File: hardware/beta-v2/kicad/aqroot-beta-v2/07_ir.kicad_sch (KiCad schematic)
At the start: 9 parts, among them Q1 AO3400A, U6 TSOP38238

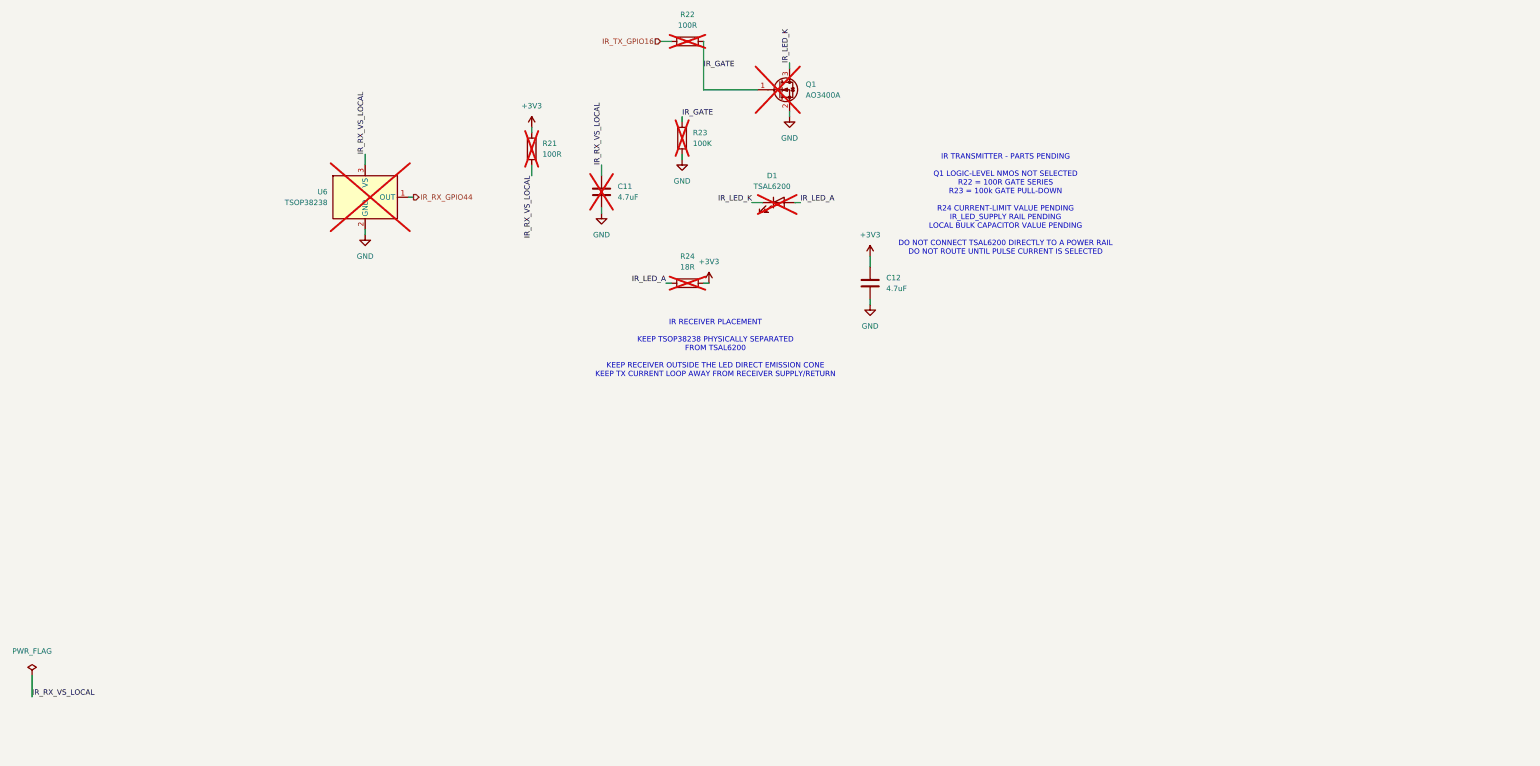
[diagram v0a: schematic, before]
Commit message: hardware: migrate Full Beta v2 infrared (FBV2-S1-007)
Sheet 07. Task gate FBV2-S1-IR = PASS.
ERC 45 -> 45: zero added, zero removed. Errors remain 2, both inherited.

THE WHOLE IR SUBSYSTEM ARRIVED DNP - FOR THE FOURTH SHEET RUNNING.

U6, D1, Q1, R21, R22, R23, R24 and C11 all came from Beta-DM marked DNP. Only
C12 was fitted - decoupling for a transmitter that was not there, exactly the
pattern found on sheet 06 with C9/C10 and the MAX98357A. The brief opens with
"Full Beta v2 IR is a mandatory internal feature", so all eight are now fitted.

Sheet 09's U16/R49/R50/U15/D2/D3, sheet 06's U5/J6, now all of sheet 07. This is
no longer a coincidence: a DNP on a Beta-DM sheet describes what was populated on
that reduced build, not what the architecture requires. Sheets 08 and 09 must be
assumed to carry the same trap.

THE RATING THAT BINDS IS NOT THE ONE THAT LOOKS BIGGEST.

IFSM = 1.5 A is a SINGLE-PULSE surge for t <= 5 us. It is not a remote-control
rating and cannot justify carrier current. The figure that governs a 38 kHz burst
train is IFM = 200 mA, specified at tp/T = 0.5 with tp = 100 us - a LONGER pulse
at the same duty than a 38 kHz carrier produces, so the carrier is less stressful
than the specified condition, not more.

Duty model, standard NEC frame ~67.5 ms with the carrier active ~22 ms at one
third duty, so the LED is on ~11 % of a frame:

  100 mA   50 % of IFM   15 mW avg   dTj 3.4 K   safe, leaves range on the table
  150 mA   75 % of IFM   25 mW avg   dTj 5.7 K   SELECTED
  200 mA  100 % of IFM   35 mW avg   dTj 8.1 K   no tolerance margin left
  300 mA  150 % of IFM        -           -      REJECTED, out of spec

Thermally none of these is difficult - 25 mW against a 160 mW PV limit on a
230 K/W part. The constraint is the repetitive rating and it is hard. Range is
not the constraint either: the TSOP384xx datasheet quotes 45 m transmission
distance using a TSAL6200 at only IF = 50 mA, and the TSAL6100 at 150 mA is
roughly 20x that intensity. Curr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
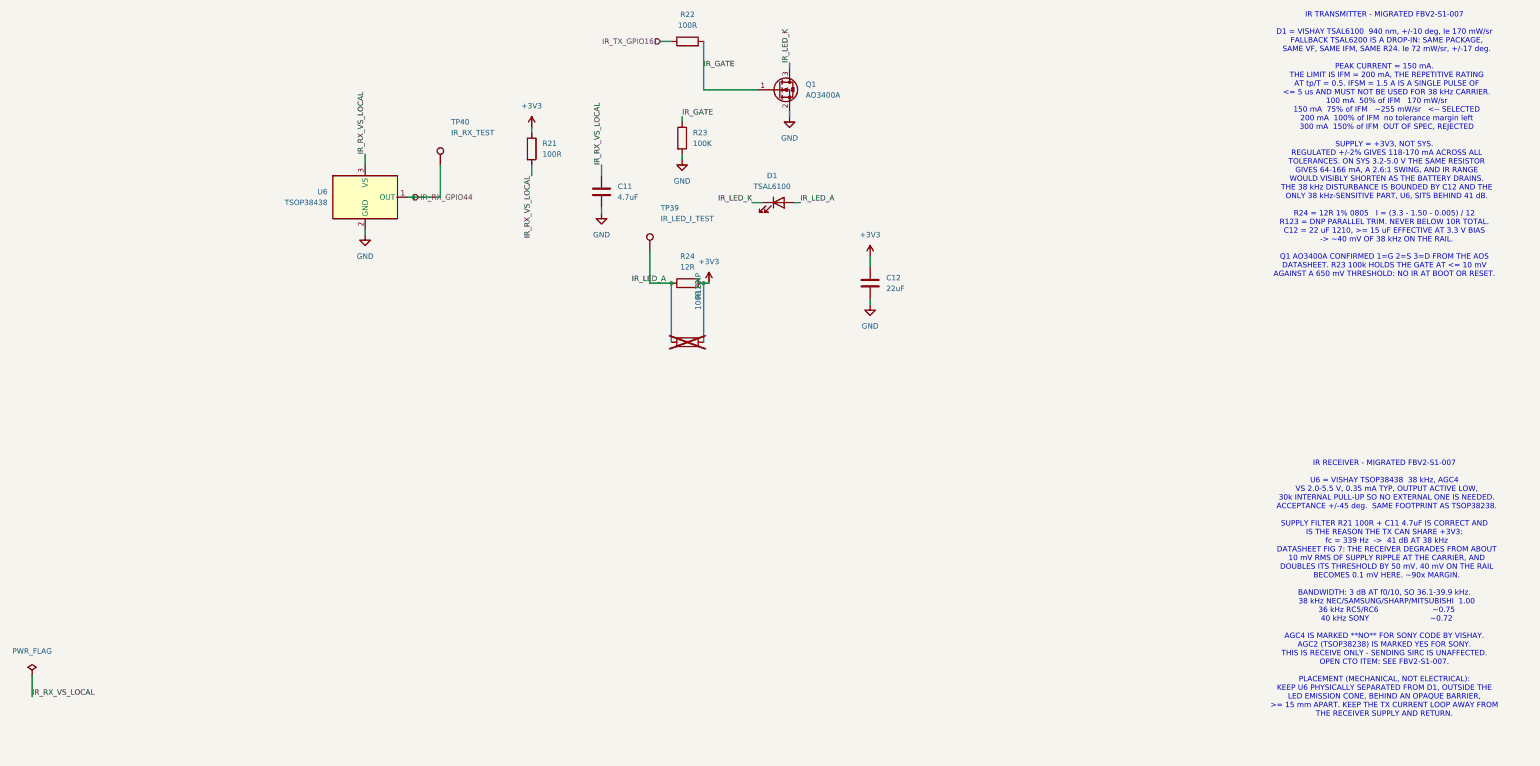
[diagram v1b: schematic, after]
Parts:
- added R123: 100R DNP, Resistor_SMD:R_0805_2012Metric, symbol Device:R
- added TP39: IR_LED_I_TEST, TestPoint:TestPoint_Pad_D1.0mm, symbol Connector:TestPoint
- added TP40: IR_RX_TEST, TestPoint:TestPoint_Pad_D1.0mm, symbol Connector:TestPoint
- C11: Note (none) -> IR RECEIVER SUPPLY FILTER, shunt element. RETAINED at 4.7 u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; now fitted
- C12: value 4.7uF -> 22uF; footprint Capacitor_SMD:C_0805_2012Metric -> Capacitor_SMD:C_1210_3225Metric; Note Local IR pulse reservoir on the +3V3 IR LED branch; supplie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 -> LOCAL IR RESERVOIR, re-derived in FBV2-S1-007. 4.7 uF -> 22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; Package 0805 (2012 metric) -> 1210 (3225 metric); Voltage 10V -> 16V
- D1: value TSAL6200 -> TSAL6100; MPN (none) -> TSAL6100; Manufacturer (none) -> Vishay; Note (none) -> IR EMITTER LOCKED TSAL6100 in FBV2-S1-007, replacing the in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; Package (none) -> T-1 3/4 leaded, 5 mm diameter, 2.54 mm lead pitch; now fitted
- Q1: Note IR LED low-side driver. Symbol Transistor_FET:Q_NMOS_GSD ma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 -> IR LED low-side driver, RETAINED after audit in FBV2-S1-007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; Package SOT-23-3 - LOCKED. Footprint BLOCKED: needs the official AO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 -> SOT-23-3, pin 1 = G, 2 = S, 3 = D (confirmed from the AOS d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; now fitted
- R21: Note (none) -> IR RECEIVER SUPPLY FILTER, series element. RETAINED at 100 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; now fitted
- R22: Note (none) -> IR gate series resistor. RETAINED at 100 R. It damps the ga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; now fitted
- R23: Note (none) -> IR gate pull-down. RETAINED at 100 k. This is the safe-OFF 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; now fitted
- R24: value 18R -> 12R; Note IR LED current limit on the +3V3 IR branch. Rail 3.3 V, TSA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 -> IR LED CURRENT LIMIT, re-derived in FBV2-S1-007 for a 150 m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; now fitted
- U6: value TSOP38238 -> TSOP38438; symbol AQROOT_Beta:TSOP38238 -> AQROOT_Beta:TSOP38438; MPN TSOP38238 -> TSOP38438; Note (none) -> RECEIVER MPN CHANGED TSOP38238 -> TSOP38438 in FBV2-S1-007 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; Package (none) -> Minicast leaded, 5.0 W x 6.95 H x 4.8 D mm, 1 = OUT, 2 = GN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; now fitted
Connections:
- net +3V3: now also R123.2
- net IR_LED_A: now also R123.1, TP39.1
- net IR_RX_GPIO44: now also TP40.1
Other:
- note added: "IR RECEIVER - MIGRATED FBV2-S1-007 U6 = VISHAY TSOP38438 38 kHz, AGC4 VS 2.0-5.5 V, 0.35 mA TYP, OUTPUT ACTIVE LOW, 30k INTERNAL PULL-UP SO NO EXTERNAL ONE IS NEEDED. ACCEPTANCE +/-45 deg. SAME FOOTPRINT AS TSOP38238. SUPPLY FILTER R21 100R + C11 4.7uF IS CORRECT AND IS THE REASON THE TX CAN SHARE +3V3: fc = 339 Hz -> 41 dB AT 38 kHz DATASHEET FIG 7: THE RECEIVER DEGRADES FROM ABOUT 10 mV RMS OF 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"
- note added: "IR TRANSMITTER - MIGRATED FBV2-S1-007 D1 = VISHAY TSAL6100 940 nm, +/-10 deg, Ie 170 mW/sr FALLBACK TSAL6200 IS A DROP-IN: SAME PACKAGE, SAME VF, SAME IFM, SAME R24. Ie 72 mW/sr, +/-17 deg. PEAK CURRENT = 150 mA. THE LIMIT IS IFM = 200 mA, THE REPETITIVE RATING AT tp/T = 0.5. IFSM = 1.5 A IS A SINGLE PULSE OF <= 5 us AND MUST NOT BE USED FOR 38 kHz CARRIER. 100 mA 50% of IFM 170 mW/sr 150 mA 75% 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"
- note removed: "IR RECEIVER PLACEMENT KEEP TSOP38238 PHYSICALLY SEPARATED FROM TSAL6200 KEEP RECEIVER OUTSIDE THE LED DIRECT EMISSION CONE KEEP TX CURRENT LOOP AWAY FROM RECEIVER SUPPLY/RETURN"
- note removed: "IR TRANSMITTER - PARTS PENDING Q1 LOGIC-LEVEL NMOS NOT SELECTED R22 = 100R GATE SERIES R23 = 100k GATE PULL-DOWN R24 CURRENT-LIMIT VALUE PENDING IR_LED_SUPPLY RAIL PENDING LOCAL BULK CAPACITOR VALUE PENDING DO NOT CONNECT TSAL6200 DIRECTLY TO A POWER RAIL DO NOT ROUTE UNTIL PULSE CURRENT IS SELECTED"

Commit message: hardware: migrate Full Beta v2 buttons expanders and RGB status
Sheet 08 migrated (FBV2-S1-008), resumed after a session-limit interruption.
All prior work was uncommitted working-tree change; it was inspected, kept and
finished rather than restarted.

Both expanders are NXP PCAL9535APW,118, verified against PCAL9535A Rev. 2
(23-Jan-2015) and NOT treated as a behavioural drop-in: it powers up with every
interrupt masked, the opposite of the TCA9535. U2 = 0x20, U3 = 0x21 preserved.

The two-expander allocation genuinely fails: 35 committed signals against 32
pins, with zero free native GPIO (so the WS2812 escape is impossible),
RESERVED_SPARE mandated by D-094 and ten XGPIO locked by D-082. Closed by U23,
a third PCAL9535APW,118 at 0x22 carrying only the front RGB and the reserved
spare - no new MPN, no new footprint, no new driver, no new rail, and B-37
retired with 12 spare I/O. Core, community and safety functions are placed
before the RGB by construction.

Landed: BQ25185_STAT1/STAT2 (10k pull-ups), SD_CARD_DETECT_N, TOUCH_INT_N,
SX1262_DIO1 on U2; ACC_3V3_EN, ACC_5V_EN, ACC_DETECT_N, ACC_POWER_FAULT_N on
U3. RESERVED_SPARE created on U23 P03 with R130 and TP41 - it had never existed.

Front RGB: D13 MEIHUA MHPA3528RGBCT (LCSC C409779), common anode, R124 1k /
R125 680R / R126 390R = 1.50 / 1.03 / 1.67 mA, white 4.20 mA. Dark by
construction with no external pull-ups.

IR receiver reverted to TSOP38238 (AGC2), TSOP38438 retained as a documented
drop-in fallback. Closes O-5.

Sheets 01 and 03 touched only to promote six local labels to hierarchical so
the required nets could reach the expanders; no component, value, topology or
DNP state changed.

ERC 42 messages / 1 error / 41 warnings - identical violation set to the
recovered tree and better than the 45/2/43 pre-sheet-08 baseline. Zero new
errors. fork_equivalence.py PASS, netclass_probe.py PASS, PCB still
bit-identical to Beta-DM. Sheet 09 untouched.

Co-Authored-By: Claude Opus 5 <noreply@anthropic.com>
Claud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
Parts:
- U6: value TSOP38438 -> TSOP38238; symbol AQROOT_Beta:TSOP38438 -> AQROOT_Beta:TSOP38238; MPN TSOP38438 -> TSOP38238; Note RECEIVER MPN CHANGED TSOP38238 -> TSOP38438 in FBV2-S1-007 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 -> RECEIVER REVERTED TSOP38438 -> TSOP38238 in FBV2-S1-008 by 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
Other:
- note added: "IR RECEIVER - MIGRATED FBV2-S1-007 RECEIVER CORRECTED FBV2-S1-008 U6 = VISHAY TSOP38238 38 kHz, AGC2 VS 2.0-5.5 V, 0.35 mA TYP, OUTPUT ACTIVE LOW, 30k INTERNAL PULL-UP SO NO EXTERNAL ONE IS NEEDED. ACCEPTANCE +/-45 deg. TSOP38438 (AGC4) IS A DOCUMENTED DROP-IN FALLBACK: SAME MINICAST BODY, SAME 1=OUT/2=GND/3=VS PINNING, SAME FOOTPRINT, SAME ELECTRICAL TABLE. SUPPLY FILTER R21 100R + C11 4.7uF IS 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"
- note removed: "IR RECEIVER - MIGRATED FBV2-S1-007 U6 = VISHAY TSOP38438 38 kHz, AGC4 VS 2.0-5.5 V, 0.35 mA TYP, OUTPUT ACTIVE LOW, 30k INTERNAL PULL-UP SO NO EXTERNAL ONE IS NEEDED. ACCEPTANCE +/-45 deg. SAME FOOTPRINT AS TSOP38238. SUPPLY FILTER R21 100R + C11 4.7uF IS CORRECT AND IS THE REASON THE TX CAN SHARE +3V3: fc = 339 Hz -> 41 dB AT 38 kHz DATASHEET FIG 7: THE RECEIVER DEGRADES FROM ABOUT 10 mV RMS OF 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"
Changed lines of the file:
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@@
 		)
 	)
-	(text "IR RECEIVER - MIGRATED FBV2-S1-007\n\nU6 = VISHAY TSOP38438  38 kHz, AGC4\n  VS 2.0-5.5 V, 0.35 mA TYP, OUTPUT ACTIVE LOW,\n  30k INTERNAL PULL-UP SO NO EXTERNAL ONE IS NEEDED.\n  ACCEPTANCE +/-45 deg.  SAME FOOTPRINT AS TSOP38238.\n\nSUPPLY FILTER R21 100R + C11 4.7uF IS CORRECT AND\nIS THE REASON THE TX CAN SHARE +3V3:\n  fc = 339 Hz  ->  41 dB AT 38 kHz\n  DATASHEET FIG 7: THE RECEIVER DEGRADES FROM ABOUT\n  10 mV RMS OF SUPPLY RIPPLE AT THE CARRIER, AND\n  DOUBLES ITS THRESHOLD BY 50 mV. 40 mV ON THE RAIL\n  BECOMES 0.1 mV HERE. ~90x MARGIN.\n\nBANDWIDTH: 3 dB AT f0/10, SO 36.1-39.9 kHz.\n  38 kHz NEC/SAMSUNG/SHARP/MITSUBISHI  1.00\n  36 kHz RC5/RC6                       ~0.75\n  40 kHz SONY                          ~0.72\n\nAGC4 IS MARKED **NO** FOR SONY CODE BY VISHAY.\nAGC2 (TSOP38238) IS MARKED YES FOR SONY.\nTHIS IS RECEIVE ONLY - SENDING SIRC IS UNAFFECTED.\nOPEN CTO ITEM: SEE FBV2-S1-007.\n\nPLACEMENT (MECHANICAL, NOT ELECTRICAL):\nKEEP U6 PHYSICALLY SEPARATED FROM D1, OUTSIDE THE\nLED EMISSION CONE, BEHIND AN OPAQUE BARRIER,\n>= 15 mm APART. KEEP THE TX CURRENT LOOP AWAY FROM\nTHE RECEIVER SUPPLY AND RETURN."
+	(text "IR RECEIVER - MIGRATED FBV2-S1-007\nRECEIVER CORRECTED FBV2-S1-008\n\nU6 = VISHAY TSOP38238  38 kHz, AGC2\n  VS 2.0-5.5 V, 0.35 mA TYP, OUTPUT ACTIVE LOW,\n  30k INTERNAL PULL-UP SO NO EXTERNAL ONE IS NEEDED.\n  ACCEPTANCE +/-45 deg.\n  TSOP38438 (AGC4) IS A DOCUMENTED DROP-IN FALLBACK:\n  SAME MINICAST BODY, SAME 1=OUT/2=GND/3=VS PINNING,\n  SAME FOOTPRINT, SAME ELECTRICAL TABLE.\n\nSUPPLY FILTER R21 100R + C11 4.7uF IS CORRECT AND\nIS THE REASON THE TX CAN SHARE +3V3:\n  fc = 339 Hz  ->  41 dB AT 38 kHz\n  DATASHEET FIG 7: THE RECEIVER DEGRADES FROM ABOUT\n  10 mV RMS OF SUPPLY RIPPLE AT THE CARRIER, AND\n  DOUBLES ITS THRESHOLD BY 50 mV. 40 mV ON THE RAIL\n  BECOMES 0.1 mV HERE. ~90x MARGIN.\n\nBANDWIDTH: 3 dB AT f0/10, SO 36.1-39.9 kHz.\n  38 kHz NEC/SAMSUNG/SHARP/MITSUBISHI  1.00\n  36 kHz RC5/RC6                       ~0.75\n  40 kHz SONY                          ~0.72\n\nO-5 IS CLOSED. THE CTO RULED FOR AGC2.\nAGC2 IS MARKED YES FOR ALL SIX LISTED PROTOCOLS\nINCLUDING SONY; AGC4 IS MARKED **NO** FOR SONY.\nMECHANISM: AFTER A BURST > 10 CYCLES AGC2 NEEDS A\nGAP > 5x THE BURST AND TAKES 10-70 CYCLES/BURST,\nAGC4 NEEDS > 15x AND TAKES ONLY 10-35. SIRC BREAKS\nTHE AGC4 LIMIT.\nCOST OF THE REVERT: AGC4 FIG 15 HIGH-MODULATION\nFLUORESCENT SUPPRESSION IS LOST. AGC2 HAS FIG 14.\n\nPLACEMENT (MECHANICAL, NOT ELECTRICAL):\nKEEP U6 PHYSICALLY SEPARATED FROM D1, OUTSIDE THE\nLED EMISSION CONE, BEHIND AN OPAQUE BARRIER,\n>= 15 mm APART. KEEP THE TX CURRENT LOOP AWAY FROM\nTHE RECEIVER SUPPLY AND RETURN."
 		(exclude_from_sim no)
 		(at 340 165 0)
@@
 	)
 	(symbol
-		(lib_id "AQROOT_Beta:TSOP38438")
+		(lib_id "AQROOT_Beta:TSOP38238")
 		(at 99.06 72.39 0)
 		(unit 1)
@@
 			)
 		)
-		(property "Value" "TSOP38438"
+		(property "Value" "TSOP38238"
 			(at 90.17 73.6599 0)
 			(show_name no)
@@
 			)
 		)
-		(property "Description" "38 kHz IR remote-control receiver module, AGC4"
+		(property "Description" "38 kHz IR remote-control receiver module, AGC2"
 			(at 99.06 72.39 0)
 			(hide yes)
@@
 			)
 		)
-		(property "MPN" "TSOP38438"
+		(property "MPN" "TSOP38238"
 			(at 99.06 72.39 0)
 			(hide yes)
@@
 			)
 		)
-		(property "Note" "RECEIVER MPN CHANGED TSOP38238 -> TSOP38438 in FBV2-S1-007 per the CTO lock. Same Minicast package, same pinning 1 = OUT / 2 = GND / 3 = VS, same footprint, so it is a pure MPN change. Verified against Vishay document 82491 Rev 2.1, 27-May-2025. VS 2.0 to 5.5 V; ISD 0.35 mA typ, 0.45 mA max at 3.3 V; output ACTIVE LOW with a 30 kOhm INTERNAL pull-up in the block diagram, so no external pull-up is needed and OUT drives GPIO44 directly; directivity plus/minus 45 deg. CARRIER AND BANDWIDTH: f0 = 38 kHz, 3 dB bandwidth f0/10, i.e. 36.1 to 39.9 kHz. Relative responsivity is 1.0 at 38 kHz (NEC, Samsung, Sharp, Mitsubishi), about 0.75 at 36 kHz (RC5/RC6) and about 0.72 at 40 kHz (Sony), costing roughly 13 to 15 percent of range on those carriers. THE 4 IS THE AGC VARIANT, NOT A PACKAGE CODE, AND IT COSTS SONY RECEPTION. Vishay marks AGC4 Preferred for NEC, RC5/RC6, Thomson RCA, Sharp and Mitsubishi and it additionally suppresses high-modulation fluorescent interference (Fig. 15) that AGC2 does not - but the same table marks AGC4 NO for Sony code, where the AGC2 TSOP38238 is marked Yes. THIS IS RECEIVE ONLY: sending Sony SIRC is unaffected because the transmitter is only a carrier and timing from the MCU. The TSOP38238 symbol is retained in the project library, so reverting to AGC2 is a lib_id change and nothing else. See FBV2-S1-007 for the open CTO item."
+		(property "Note" "RECEIVER REVERTED TSOP38438 -> TSOP38238 in FBV2-S1-008 by CTO ruling on the O-5 item raised at FBV2-S1-007. TSOP38238 is the AGC2 part and is the FITTED first build; TSOP38438 (AGC4) is retained as a DOCUMENTED DROP-IN FALLBACK and its symbol stays in the project library. Verified against Vishay document 82491 Rev 2.1, 27-May-2025: both MPNs appear in the SAME parts table sharing the Minicast package, the pinning 1 = OUT / 2 = GND / 3 = VS, the body 5.0 W x 6.95 H x 4.8 D mm, leaded mounting and one shared electrical table - so this is a pure MPN change and the footprint, the R21/C11 supply filter and every FBV2-S1-007 calculation are unaffected. VS 2.0 to 5.5 V; ISD 0.25 / 0.35 / 0.45 mA at VS = 3.3 V; output ACTIVE LOW with a 30 kOhm INTERNAL pull-up so OUT drives GPIO44 directly and no external pull-up is needed; directivity plus/minus 45 deg; f0 = 38 kHz with a 3 dB bandwidth of f0/10, i.e. 36.1 to 39.9 kHz. WHY AGC2 IS THE RIGHT FIRST BUILD: the suitable-data-format table marks AGC2 Yes for NEC, RC5/RC6, Thomson RCA 56 kHz, Sharp, SONY and Mitsubishi, where AGC4 is marked NO for Sony code. The mechanism is the gap requirement - after a burst longer than 10 cycles AGC2 needs a gap of more than 5 x the burst length and accepts 10 to 70 cycles per burst, while AGC4 needs more than 15 x and accepts only 10 to 35 - and Sony SIRC violates the AGC4 limit. WHAT IS GIVEN UP: AGC4 adds the Fig. 15 suppression of high-modulation fluorescent-lamp interference that AGC2 (Fig. 14 only) does not have. That is the whole cost of the revert, and it is a fluorescent-lighting robustness margin rather than a protocol."
 			(at 99.06 72.39 0)
 			(hide yes)

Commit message: hardware: close Full Beta v2 S2 release blockers
Closes B-03, B-63, B-70 and B-71's schematic-side work. Property-only
changes to the nine sheets plus the microphone footprint; ERC unchanged
at 27 / 0 errors / 27 with an identical violation histogram, and the PCB
is untouched and still bit-identical to Beta-DM.

B-03 - all eight remaining Tier-2 footprints compared dimension by
dimension against retrieved manufacturer drawings. Y1 moves from
candidate to lock (Yajingxin TXM27.12M0004322DBBDO00T, C362365, 3421 in
stock) with a land that matches the vendor's Suggested Layout exactly.
The MAX98357A looked like a genuine defect - outline 21-0136 gives
T1633-5 an EP of 1.50/1.60/1.70 while the land is 1.23 - and is not:
land pattern 90-0032 Rev E is issued for T1633-5, -5C and -7C together
and specifies one land for all three, so no project-local footprint was
created.

B-63 - the microphone acoustic port is now drawn rather than described.
1.05 mm NPTH taken from the drawing's own pad-4 ring inner diameter,
paste pulled back 0.10 mm as a declared stencil choice, keepout marked,
bottom-port orientation recorded.

B-70 - L5/L6 lock to Murata LQW18AN39NG80D. The DCR is a first-order
term here: 0.20 ohm max against R_q = 1.1 ohm drops network Q from 25.3
to about 21.4, so the antenna must be tuned with this exact part fitted
and the first lever is R_q, not 39 nH.

B-71 - 65 LCSC fields written in, three MPN strings corrected. J6 and J7
carried bare order codes that resolve to zero-stock listings while the
plating-suffixed strings are abundantly stocked. Six substitution traps
recorded in the symbols themselves, including BAT54W offered for
BAT54WS - a single diode for a series pair - and a clone for the battery
reverse-polarity pass FETs.

Eight DNP parts still carried no recorded reason and now do. The design
has zero unexplained DNP.

Co-Authored-By: Claude Opus 5 <noreply@anthropic.com>
Claude-Session: https://claude.ai/code/session_0133CdFHfKcCH8oPWqJZWe7o
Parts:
- D1: LCSC (none) -> C111836
- U6: LCSC (none) -> C141632
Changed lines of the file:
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@@
+			)
+		)
+		(property "LCSC" "C141632"
+			(at 99.06 72.39 0)
+			(hide yes)
+			(show_name no)
+			(do_not_autoplace no)
+			(effects
+				(font
+					(size 1.27 1.27)
+				)
 			)
 		)
@@
 			(at 196.85 73.66 0)
 			(hide yes)
+			(show_name no)
+			(do_not_autoplace no)
+			(effects
+				(font
+					(size 1.27 1.27)
+				)
+			)
+		)
+		(property "LCSC" "C111836"
+			(at 196.85 73.66 0)
+			(hide yes)
